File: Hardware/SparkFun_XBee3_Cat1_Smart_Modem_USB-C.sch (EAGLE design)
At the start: 50 parts, among them J3 USB Female Type C Connector, J4 QWIIC_RIGHT_ANGLE, U2 AP63203, U5 ESD Diode, U6 CP210X

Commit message: General placement of parts
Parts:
- added D1, D5: 3A/10V/280mV, SparkFun-DiscreteSemi:DIODE-SCHOTTKY-BAT60A
- added J1: USB Female Type C Connector, SparkFun-Connectors:USB_C_4-LAYER-ISOLATED
- added R1: 100k, SparkFun-Resistors:100KOHM-0603-1/10W-1%
- added R13, R16: 5.1k, SparkFun-Resistors:5.1KOHM5.1KOHM-0603-1/10W-1%
- added S3: (no value), SparkFun-Switches:SWITCH-DPDT-SMD-AYZ0202
- added SHLD1: JUMPER-SMT_2_NC_TRACE_SILK, SparkFun-Jumpers:JUMPER-SMT_2_NC_TRACE_SILK
- added U1: FSUSB30MUX_MSOP10, SparkFun-IC-Special-Function:FSUSB30MUX_MSOP10
- added U3: ESD Diode, SparkFun-DiscreteSemi:TVS_DIODE_ARRAY_DT1042-04SO-7
- R11: device SparkFun-Resistors:1KOHM-0402T-1/16W-1% -> SparkFun-Resistors:1KOHM-0603-1/10W-1%
- R12, R2: device SparkFun-Resistors:2.2KOHM-0402T-1/16W-1% -> SparkFun-Resistors:2.2KOHM-0603-1/10W-1%
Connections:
- removed net N$17: B1.D12
- removed net N$20: B1.*D9
- removed net N$22: B1.D8
- removed net N$24: B1.D7
- removed net N$25: B1.*D6
- removed net N$4: J2.D-
- new net DIRECT_D+: J1.D+, U1.D2+, U3.IO4
- new net DIRECT_D-: J1.D-, U1.D2-, U3.IO3
- new net DIRECT_SELECT: S3.2, S3.5, U1.S
- new net FIRMWARE: R1.2, S3.1, S3.4
- new net N$14: J1.CC2, R16.2
- new net N$15: J1.CC1, R13.2
- new net SHLD1: J1.SHLD, SHLD1.2
- new net V_USB_2: D1.A, J1.VBUS, U3.VCC
- new net XBEE_D+/SDA: J2.D+/SDA/DIO11, U1.D+
- new net XBEE_D-: J2.D-, U1.D-
- net 3.3V: now also R1.1, U1.VCC
- net D11/SDA: now also U1.D1+; no longer J2.D+/SDA/DIO11
- net D12/SPI_POCI: now also B1.D12
- net D6/!RTS!: now also B1.*D6
- net D7/!CTS!: now also B1.D7
- net D8/!DTR!: now also B1.D8
- net D9/!SLEEP!: now also B1.*D9
- net GND: now also J1.GND, R13.1, R16.1, S3.3, S3.6, SHLD1.1, U1.!OE!, U1.GND, U3.VSS
- net VIN: now also D1.C, D5.C
- net V_USB: now also D5.A
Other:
- moved on the sheet: I2C_PU, J3, J4, R14, R15, R7, R8, SHLD, U5

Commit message: More changes to part placement
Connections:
- net N$27 renamed D4_SPI_PICO
- removed net N$16: B1.D13
- removed net N$28: B1.*D3
- removed net N$29: B1.D2
- removed net N$35: B1.AREF
- removed net N$37: B1.5V
- removed net N$38: B1.VIN
- removed net N$39: B1.RES
- removed net N$40: B1.IOREF
- removed net N$41: B1.A5
- removed net N$42: B1.A4
- removed net N$43: B1.A3
- removed net N$44: B1.A2
- removed net N$45: B1.A1
- removed net N$46: B1.A0
- net D0: now also B1.A0
- net D11/SDA: no longer B1.*D11
- net D2/SPI_CLK: now also B1.D2
- net D3/SPI_!CS!: now also B1.*D3
- net VIN: now also B1.VIN
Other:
- moved on the sheet: B1, C1, C2, C3, C4, C5, C8, D1, D5, I2C_PU, J4, L1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

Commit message: Rearranges USB-C and Qwiic connectors
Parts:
- removed J7: (no value), SparkFun-Connectors:CONN_021X02_NO_SILK
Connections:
- net EN: now also B1.*D11; no longer J7.1
- net VIN: no longer J7.2
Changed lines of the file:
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@@
 <part name="RLED" library="SparkFun-Jumpers" deviceset="JUMPER-SMT_2_NC_TRACE" device="_SILK" package3d_urn="urn:adsk.eagle:package:39281/1"/>
 <part name="SUPPLY23" library="SparkFun-PowerSymbols" deviceset="3.3V" device=""/>
-<part name="SUPPLY24" library="SparkFun-PowerSymbols" deviceset="VIN" device=""/>
 <part name="GND17" library="SparkFun-PowerSymbols" deviceset="GND" device=""/>
-<part name="J7" library="SparkFun-Connectors" deviceset="CONN_02" device="1X02_NO_SILK"/>
 <part name="J3" library="SparkFun-Connectors" deviceset="USB_C" device="_4-LAYER-ISOLATED" value="USB Female Type C Connector"/>
 <part name="GND4" library="SparkFun-PowerSymbols" deviceset="GND" device=""/>
@@
 <attribute name="NAME" x="203.2" y="93.472" size="1.778" layer="95" font="vector" rot="R180" align="center"/>
 </instance>
-<instance part="SUPPLY23" gate="G$1" x="261.62" y="55.88" smashed="yes">
-<attribute name="VALUE" x="261.62" y="58.674" size="1.778" layer="96" font="vector" align="bottom-center"/>
-</instance>
-<instance part="SUPPLY24" gate="G$1" x="266.7" y="55.88" smashed="yes">
-<attribute name="VALUE" x="266.7" y="58.674" size="1.778" layer="96" font="vector" align="bottom-center"/>
+<instance part="SUPPLY23" gate="G$1" x="261.62" y="48.26" smashed="yes">
+<attribute name="VALUE" x="261.62" y="51.054" size="1.778" layer="96" font="vector" align="bottom-center"/>
 </instance>
 <instance part="GND17" gate="1" x="266.7" y="17.78" smashed="yes" rot="MR0">
 <attribute name="VALUE" x="266.7" y="17.526" size="1.778" layer="96" font="vector" rot="MR0" align="top-center"/>
-</instance>
-<instance part="J7" gate="G$1" x="251.46" y="50.8" smashed="yes">
-<attribute name="VALUE" x="248.92" y="45.974" size="1.778" layer="96" font="vector"/>
-<attribute name="NAME" x="248.92" y="56.388" size="1.778" layer="95" font="vector"/>
 </instance>
 <instance part="J3" gate="J1" x="325.12" y="248.92" smashed="yes">
@@
 </segment>
 <segment>
-<wire x1="264.16" y1="30.48" x2="259.08" y2="30.48" width="0.1524" layer="91"/>
-<label x="264.16" y="30.48" size="1.27" layer="95" font="vector" xref="yes"/>
+<wire x1="261.62" y1="30.48" x2="259.08" y2="30.48" width="0.1524" layer="91"/>
+<label x="261.62" y="30.48" size="1.27" layer="95" font="vector" xref="yes"/>
 <pinref part="J6" gate="J1" pin="7"/>
 </segment>
@@
 </segment>
 <segment>
-<wire x1="261.62" y1="45.72" x2="261.62" y2="55.88" width="0.1524" layer="91"/>
+<wire x1="261.62" y1="45.72" x2="261.62" y2="48.26" width="0.1524" layer="91"/>
 <wire x1="259.08" y1="45.72" x2="261.62" y2="45.72" width="0.1524" layer="91"/>
 <pinref part="SUPPLY23" gate="G$1" pin="3.3V"/>
@@
 </segment>
 <segment>
-<wire x1="264.16" y1="43.18" x2="259.08" y2="43.18" width="0.1524" layer="91"/>
-<label x="264.16" y="43.18" size="1.27" layer="95" font="vector" xref="yes"/>
+<wire x1="261.62" y1="43.18" x2="259.08" y2="43.18" width="0.1524" layer="91"/>
+<label x="261.62" y="43.18" size="1.27" layer="95" font="vector" xref="yes"/>
 <pinref part="J6" gate="J1" pin="2"/>
 </segment>
@@
 </segment>
 <segment>
-<wire x1="264.16" y1="40.64" x2="259.08" y2="40.64" width="0.1524" layer="91"/>
-<label x="264.16" y="40.64" size="1.27" layer="95" font="vector" xref="yes"/>
+<wire x1="261.62" y1="40.64" x2="259.08" y2="40.64" width="0.1524" layer="91"/>
+<label x="261.62" y="40.64" size="1.27" layer="95" font="vector" xref="yes"/>
 <pinref part="J6" gate="J1" pin="3"/>
 </segment>
@@
 </segment>
 <segment>
-<wire x1="264.16" y1="38.1" x2="259.08" y2="38.1" width="0.1524" layer="91"/>
-<label x="264.16" y="38.1" size="1.27" layer="95" font="vector" xref="yes"/>
+<wire x1="261.62" y1="38.1" x2="259.08" y2="38.1" width="0.1524" layer="91"/>
+<label x="261.62" y="38.1" size="1.27" layer="95" font="vector" xref="yes"/>
 <pinref part="J6" gate="J1" pin="4"/>
 </segment>
@@
 </segment>
 <segment>
-<wire x1="264.16" y1="35.56" x2="259.08" y2="35.56" width="0.1524" layer="91"/>
-<label x="264.16" y="35.56" size="1.27" layer="95" font="vector" xref="yes"/>
+<wire x1="261.62" y1="35.56" x2="259.08" y2="35.56" width="0.1524" layer="91"/>
+<label x="261.62" y="35.56" size="1.27" layer="95" font="vector" xref="yes"/>
 <pinref part="J6" gate="J1" pin="5"/>
 </segment>
@@
 </segment>
 <segment>
-<wire x1="264.16" y1="33.02" x2="259.08" y2="33.02" width="0.1524" layer="91"/>
-<label x="264.16" y="33.02" size="1.27" layer="95" font="vector" xref="yes"/>
+<wire x1="261.62" y1="33.02" x2="259.08" y2="33.02" width="0.1524" layer="91"/>
+<label x="261.62" y="33.02" size="1.27" layer="95" font="vector" xref="yes"/>
 <pinref part="J6" gate="J1" pin="6"/>
 </segment>
@@
 </segment>
 <segment>
-<wire x1="264.16" y1="25.4" x2="259.08" y2="25.4" width="0.1524" layer="91"/>
-<label x="264.16" y="25.4" size="1.27" layer="95" font="vector" xref="yes"/>
+<wire x1="261.62" y1="25.4" x2="259.08" y2="25.4" width="0.1524" layer="91"/>
+<label x="261.62" y="25.4" size="1.27" layer="95" font="vector" xref="yes"/>
 <pinref part="J6" gate="J1" pin="9"/>
 </segment>
@@
 </net>
 <net name="VIN" class="0">
-<segment>
-<wire x1="259.08" y1="53.34" x2="266.7" y2="53.34" width="0.1524" layer="91"/>
-<wire x1="266.7" y1="53.34" x2="266.7" y2="55.88" width="0.1524" layer="91"/>
-<pinref part="SUPPLY24" gate="G$1" pin="VIN"/>
-<pinref part="J7" gate="G$1" pin="2"/>
-</segment>
 <segment>
 <pinref part="R17" gate="G$1" pin="2"/>
@@
 </segment>
 <segment>
-<wire x1="264.16" y1="50.8" x2="259.08" y2="50.8" width="0.1524" layer="91"/>
-<label x="264.16" y="50.8" size="1.27" layer="95" font="vector" xref="yes"/>
-<pinref part="J7" gate="G$1" pin="1"/>
-</segment>
-</net>
+<pinref part="B1" gate="G$1" pin="*D11"/>
+<wire x1="289.56" y1="96.52" x2="287.02" y2="96.52" width="0.1524" layer="91"/>
+<label x="289.56" y="96.52" size="1.27" layer="95" xref="yes"/>
+</segment>
+</net>

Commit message: Routes more stuff
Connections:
- removed net D4_SPI_PICO: B1.D4
- net D4/SPI_PICO: now also B1.D4
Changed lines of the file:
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@@
 <pinref part="J5" gate="J1" pin="10"/>
+</segment>
+<segment>
+<pinref part="B1" gate="G$1" pin="D4"/>
+<wire x1="289.56" y1="114.3" x2="287.02" y2="114.3" width="0.1524" layer="91"/>
+<label x="289.56" y="114.3" size="1.27" layer="95" font="vector" xref="yes"/>
 </segment>
 </net>
@@
 </segment>
 </net>
-<net name="D4_SPI_PICO" class="0">
-<segment>
-<pinref part="B1" gate="G$1" pin="D4"/>
-<wire x1="289.56" y1="114.3" x2="287.02" y2="114.3" width="0.1524" layer="91"/>
-<label x="289.56" y="114.3" size="1.27" layer="95" font="vector" xref="yes"/>
-</segment>
-</net>

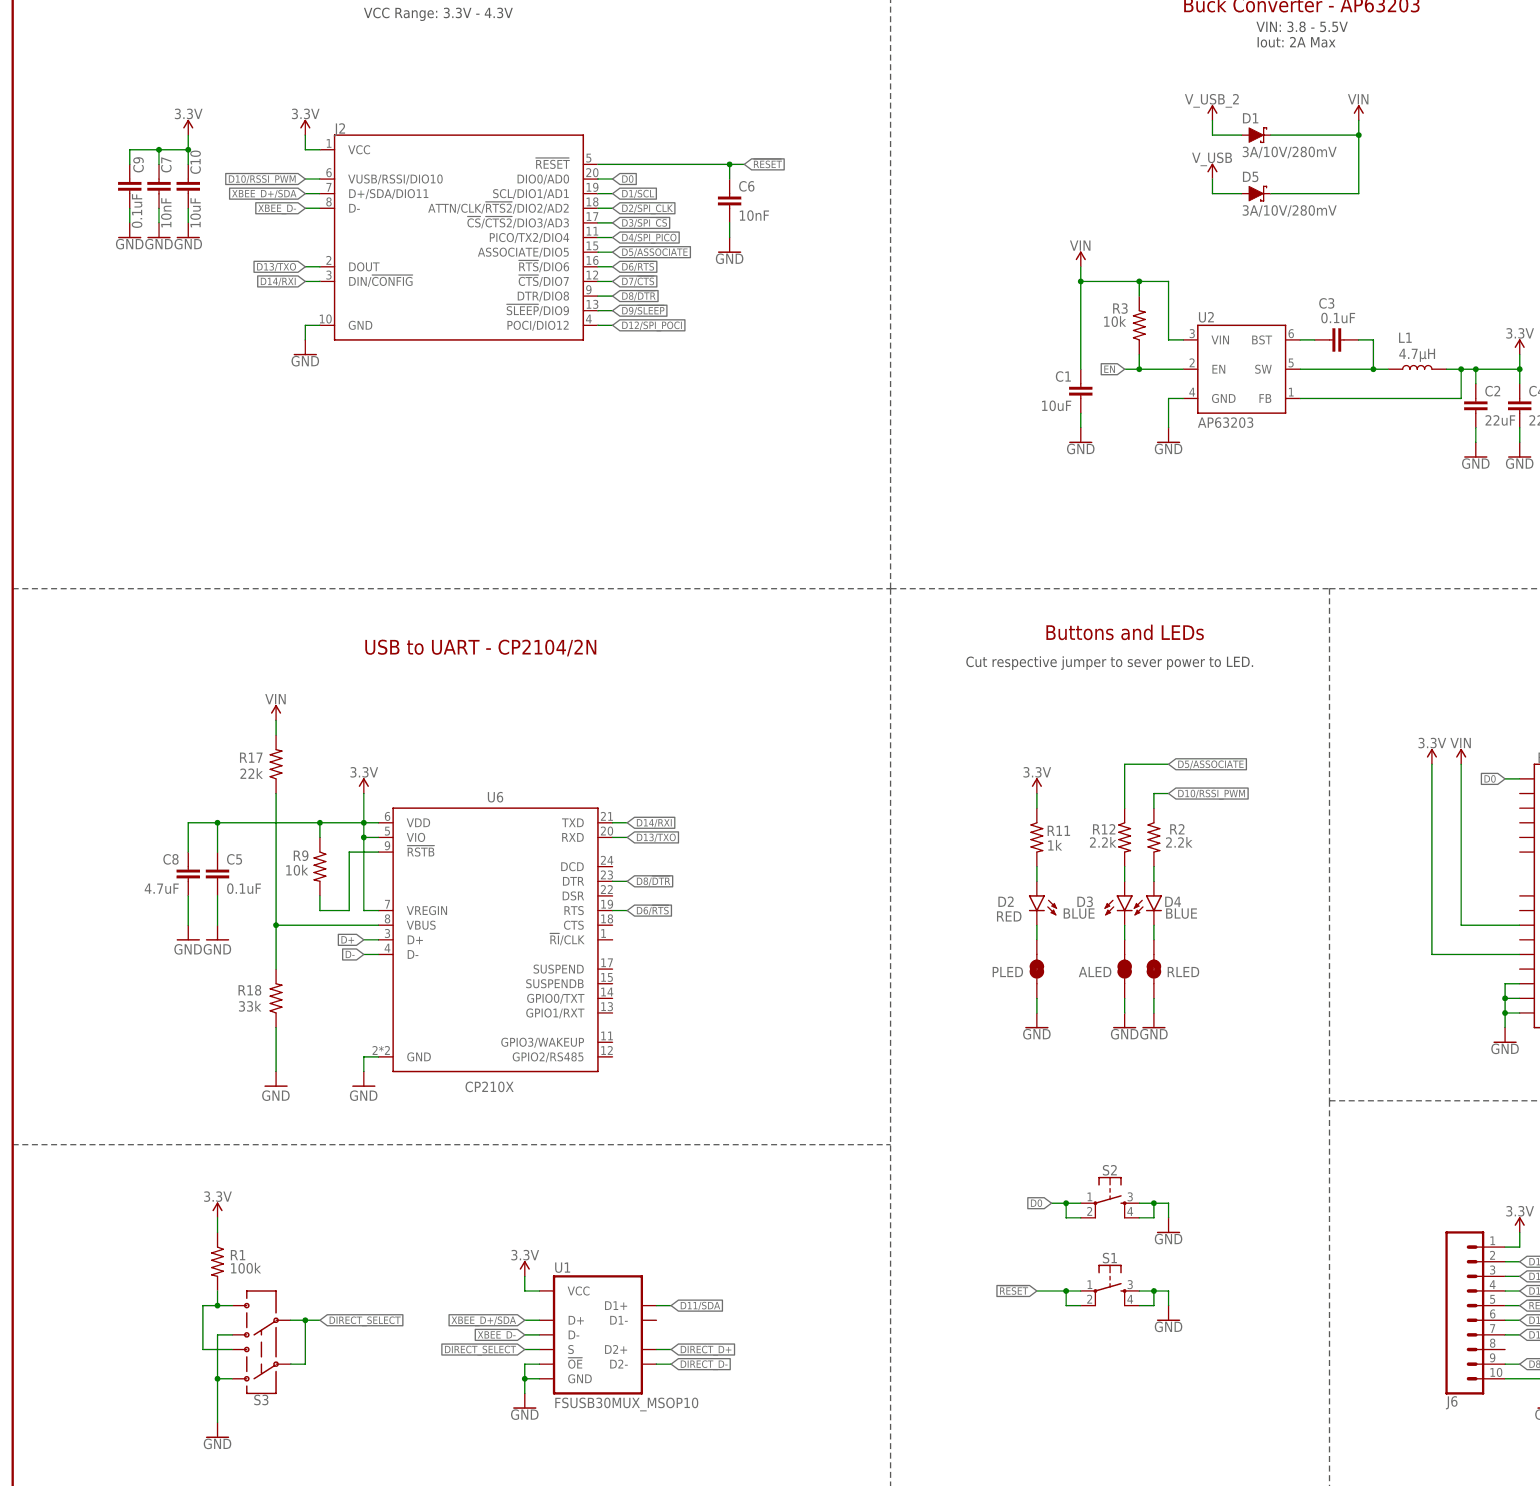
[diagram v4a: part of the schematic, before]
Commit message: Adds FT231XS, pushes all signals to bottom layer that were on layer two
* Adds decoupling cap and 100 Ohm resistor to UART MUX
* Moves some silk around
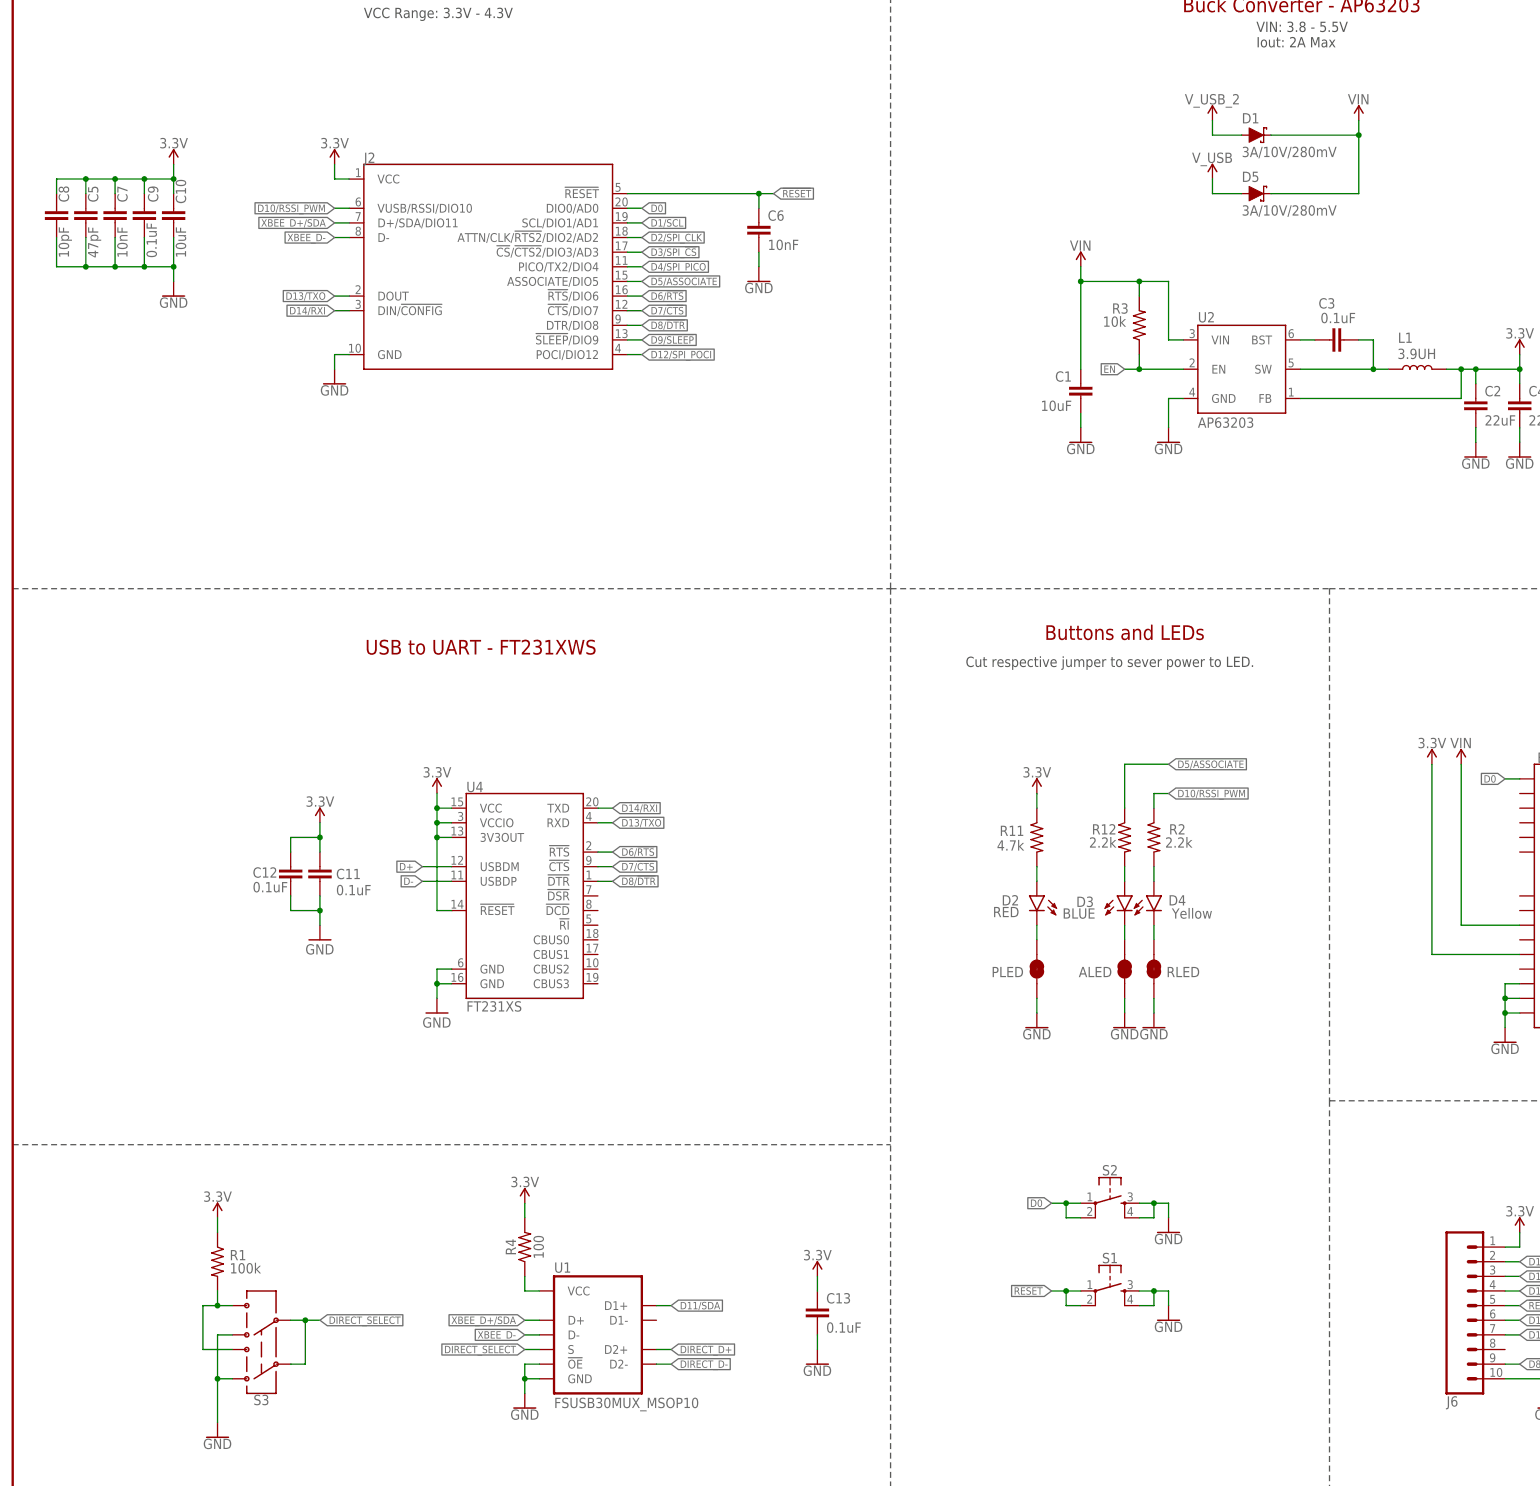
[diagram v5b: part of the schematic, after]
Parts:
- removed R17: 22k, SparkFun-Resistors:22KOHM-0603-1/10W-1%
- removed R18: 33k, SparkFun-Resistors:33KOHM-0603-1/10W-1%
- removed R9: 10k, SparkFun-Resistors:10KOHM-0603-1/10W-1%
- removed U6: CP210X, SparkFun-IC-Comms:CP2102N
- added C11, C12, C13: 0.1uF, SparkFun-Capacitors:0.1UF-0603-25V-(+80/-20%)
- added R4: 100, SparkFun-Resistors:100OHM-0603-1/10W-1%
- added U4: FT231XS, SparkFun-IC-Comms:FT231XS
- C5: value 0.1uF -> 47pF; device SparkFun-Capacitors:0.1UF-0603-25V-(+80/-20%) -> SparkFun-Capacitors:47PF-0603-50V-5%
- C8: value 4.7uF -> 10pF; device SparkFun-Capacitors:4.7UF-0603-6.3V-(10%) -> SparkFun-Capacitors:10PF-0603-50V-5%
- D2: device SparkFun-LED:LED-RED0603 -> SparkFun-LED:LED-RED_0603-KB
- D4: value BLUE -> Yellow; device SparkFun-LED:LED-BLUE0603 -> SparkFun-LED:LED-YELLOW0603
- L1: value 4.7μH -> 3.9UH; device SparkFun-Coils:4.7μH_SHIELDED_INDUCTORNPIS_LS -> SparkFun-Coils:3.9UH
- R11: value 1k -> 4.7k; device SparkFun-Resistors:1KOHM-0603-1/10W-1% -> SparkFun-Resistors:4.7KOHM-0603-1/10W-1%
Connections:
- removed net N$9: R9.2, U6.!RSTB
- net 3.3V: now also C11.1, C12.1, C13.1, R4.2, U4.!RESET, U4.3V3OUT, U4.VCC, U4.VCCIO; no longer R9.1, U1.VCC, U6.VDD, U6.VIO, U6.VREGIN
- net D+: now also U4.USBDM; no longer U6.D+
- net D-: now also U4.USBDP; no longer U6.D-
- net D13/TXO: now also U4.RXD; no longer U6.RXD
- net D14/RXI: now also U4.TXD; no longer U6.TXD
- net D6/!RTS!: now also U4.!RTS; no longer U6.RTS
- net D7/!CTS!: now also U4.!CTS
- net D8/!DTR!: now also U4.!DTR; no longer U6.DTR
- net GND: now also C11.2, C12.2, C13.2, U4.GND@16, U4.GND@6; no longer R18.1, U6.GND
- net N$10: now also R4.1, U1.VCC; no longer R17.1, R18.2, U6.VBUS
- net VIN: no longer R17.2
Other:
- note added: "USB to UART - FT231XWS"
- note removed: "USB to UART - CP2104/2N"
- moved on the sheet: C10, C5, C6, C7, C8, C9, J2
